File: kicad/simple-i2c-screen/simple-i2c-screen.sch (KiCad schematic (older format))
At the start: 29 parts, among them J1 Barrel_Jack_MountingPin, J2 Conn_01x06, J3 Conn_01x01, J4 RJ12, J5 Conn_01x01, J6 Conn_01x01, J7 Conn_01x01, J8 Conn_02x03_Odd_Even, U1 LM78M05_TO252

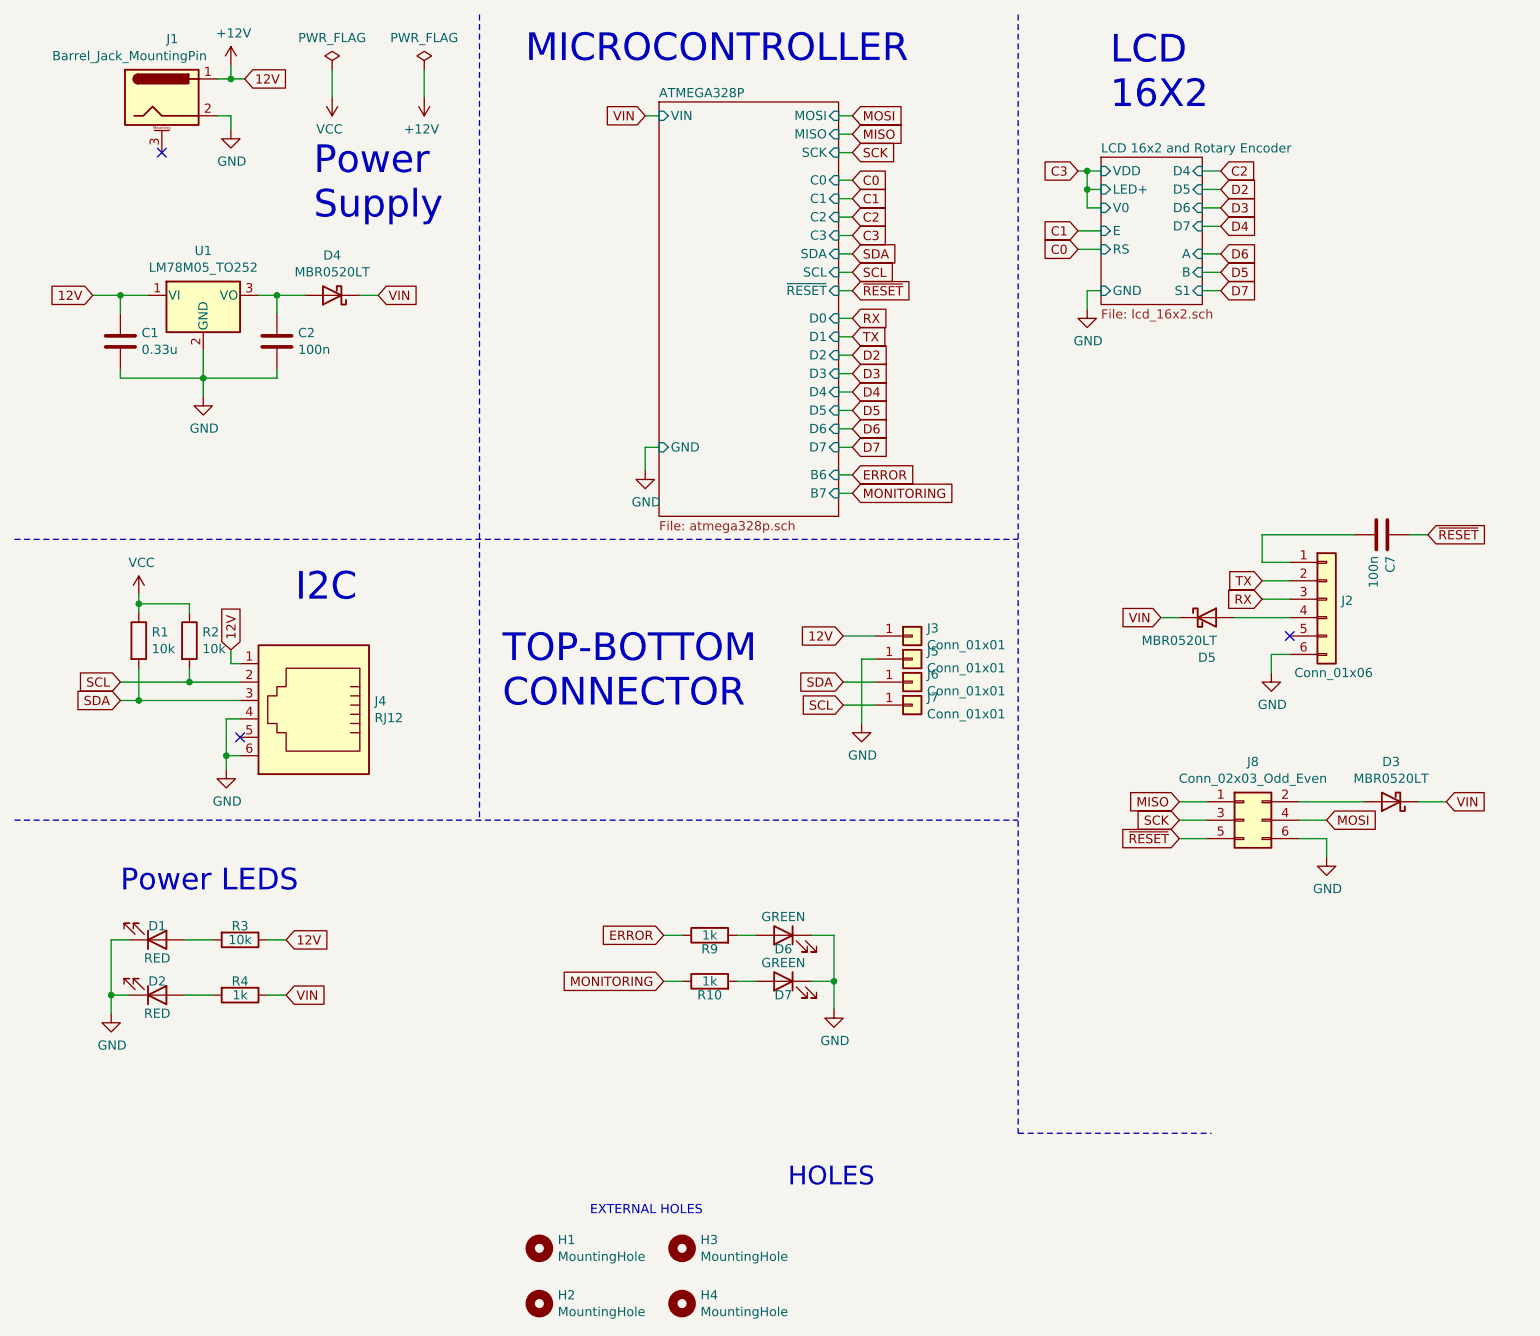
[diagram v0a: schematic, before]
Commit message: refactor: version 1.0.3 for PCB change MOITORING_LED to pin 13 like Arduino
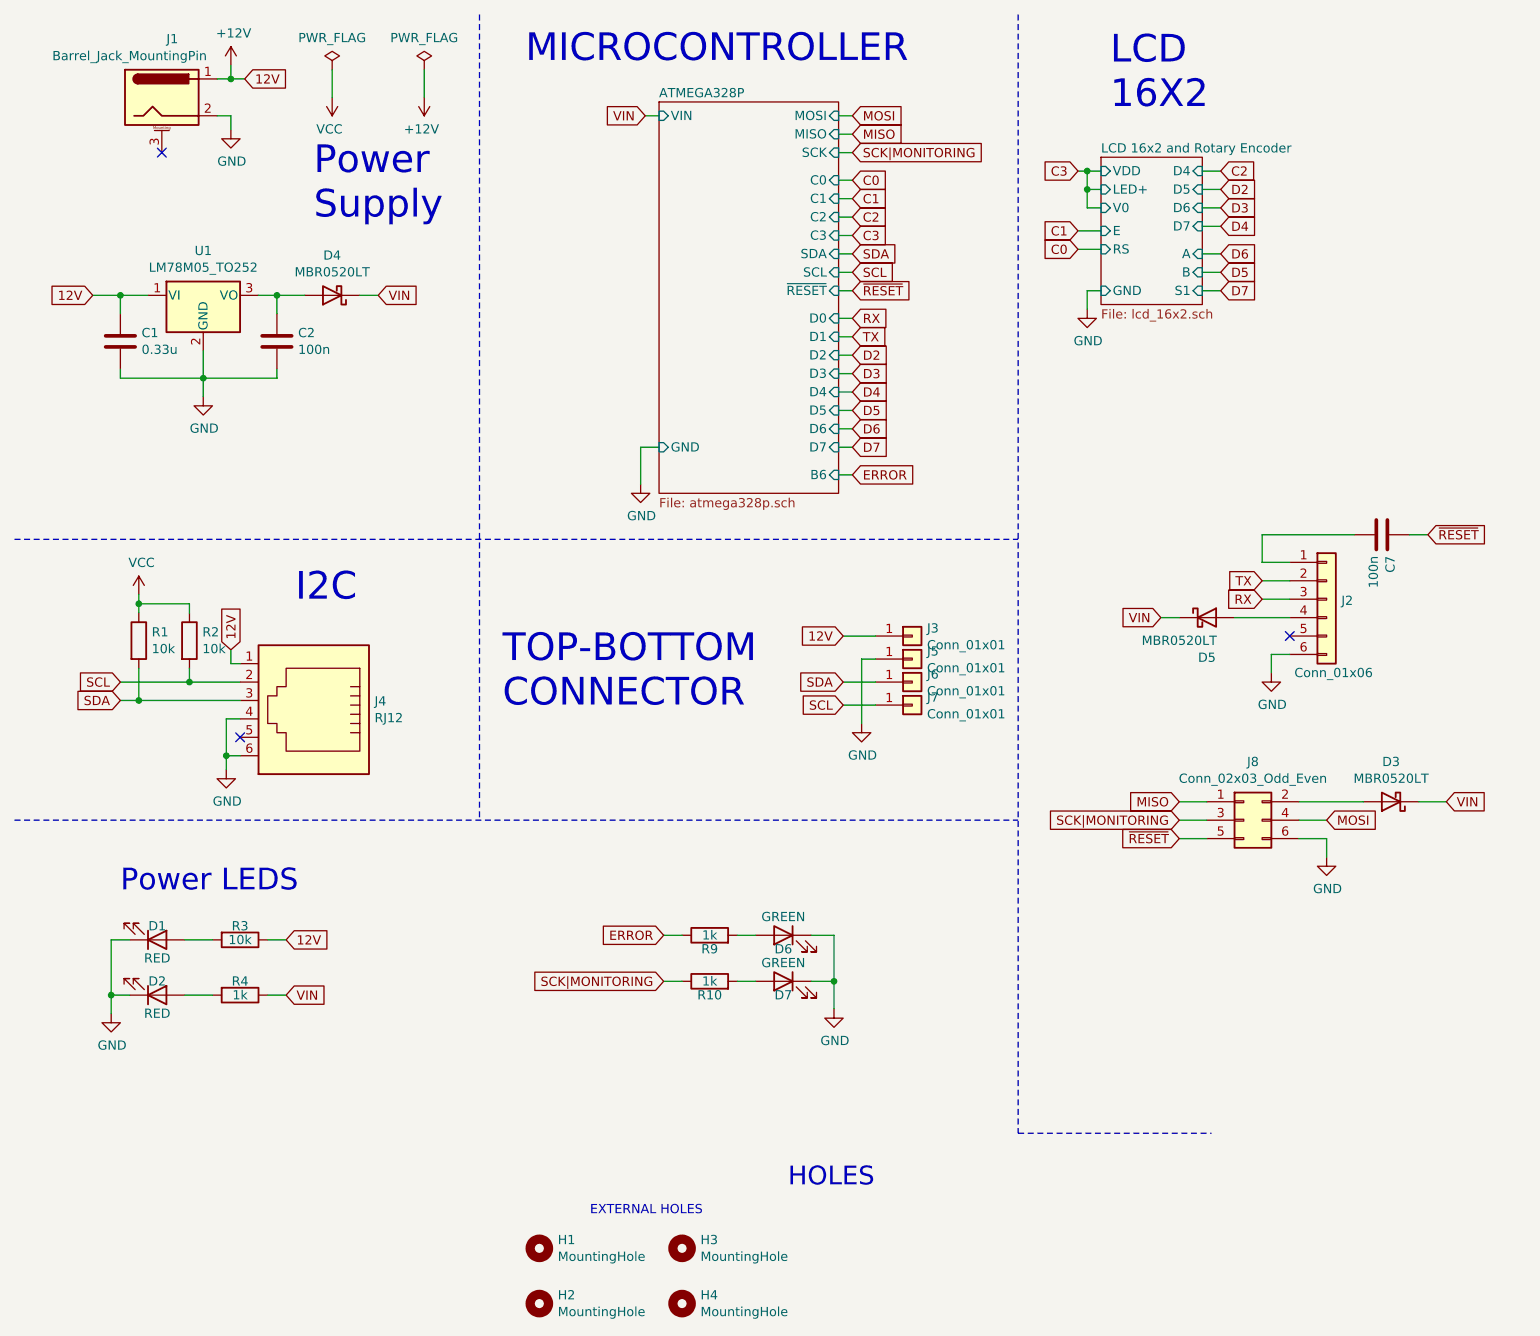
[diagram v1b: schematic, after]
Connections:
- net SCK is gone; now on net SCK|MONITORING: J8.3 (Pin_3)
- net MONITORING renamed SCK|MONITORING
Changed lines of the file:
@@
 SDA
 Text GLabel 5025 1225 2    50   Input ~ 0
-SCK
+SCK|MONITORING
 Text GLabel 5025 1125 2    50   Input ~ 0
 MISO
@@
 L incubator-rescue:GND-power #PWR0105
 U 1 1 6100E2AC
-P 3900 2950
-F 0 "#PWR0105" H 3900 2700 50  0001 C CNN
-F 1 "GND" H 3905 2777 50  0000 C CNN
-F 2 "" H 3900 2950 50  0001 C CNN
-F 3 "" H 3900 2950 50  0001 C CNN
-	1    3900 2950
+P 3875 3025
+F 0 "#PWR0105" H 3875 2775 50  0001 C CNN
+F 1 "GND" H 3880 2852 50  0000 C CNN
+F 2 "" H 3875 3025 50  0001 C CNN
+F 3 "" H 3875 3025 50  0001 C CNN
+	1    3875 3025
 	1    0    0    -1
 $EndComp
 Wire Wire Line
 	3900 1025 3975 1025
-Wire Wire Line
-	3975 2825 3900 2825
-Wire Wire Line
-	3900 2825 3900 2950
 $Comp
 L incubator-rescue:GND-power #PWR0114
@@
 MISO
 Text GLabel 6800 4850 0    50   Input ~ 0
-SCK
+SCK|MONITORING
 Text GLabel 6800 4950 0    50   Input ~ 0
 ~RESET
@@
 Text GLabel 5025 2975 2    50   Input ~ 0
 ERROR
-Text GLabel 5025 3075 2    50   Input ~ 0
-MONITORING
 Wire Wire Line
 	4950 2975 5025 2975
-Wire Wire Line
-	5025 3075 4950 3075
 Text GLabel 4000 5475 0    50   Input ~ 0
 ERROR
 Text GLabel 4000 5725 0    50   Input ~ 0
-MONITORING
+SCK|MONITORING
 Wire Wire Line
 	4100 5725 4000 5725
@@
 	4925 5475 4925 5725
 $Sheet
-S 3975 950  975  2250
+S 3975 950  975  2125
 U 61116939
 F0 "ATMEGA328P" 50
@@
 F21 "SCK" I R 4950 1225 50
 F22 "B6" I R 4950 2975 50
-F23 "B7" I R 4950 3075 50
 $EndSheet
 $Sheet
@@
 F14 "V0" I L 6375 1525 50
 $EndSheet
+Wire Wire Line
+	3875 2825 3975 2825
+Wire Wire Line
+	3875 2825 3875 3025
 $EndSCHEMATC
